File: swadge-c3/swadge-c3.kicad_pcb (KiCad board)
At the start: 2 copper layers, 62 parts, among them J1 USB_B_Micro, SW1 SW_SPDT, SW2 4-1437565-2, SW3 4-1437565-2, SW4 4-1437565-2, SW5 4-1437565-2, SW6 4-1437565-2, SW7 4-1437565-2, SW8 4-1437565-2, SW9 4-1437565-2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

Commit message: Updated schematic
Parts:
- added C21: 2.2u, Swadge_Parts:C_0603_1608Metric, F.Cu at (169.8, 122.4)
- added D7: WS2812B, Swadge_Parts:LED_WS2812B_PLCC4_5.0x5.0mm_P3.2mm, F.Cu at (171.8, 117.9)
- added D8: WS2812B, Swadge_Parts:LED_WS2812B_PLCC4_5.0x5.0mm_P3.2mm, F.Cu at (179.8, 117.9)
- C10: value 0.1uF -> 10uF
- C11: value 1uF -> 0.1uF
- C12: value 1u -> 1uF
- C16: value 2.2u -> 1u
- C17: value 10u -> 2.2u
- C18: value 0.01u -> 10u
- C19: value 0.1u -> 0.01u
- C20: value 2.2u -> 0.1u
- C9: value 10uF -> 1u
- R12: value 10K -> 390k
- R9: value 390k -> 10K
- SW1: value SW_SPDT -> 4-1437565-2; footprint Swadge_Parts:SW_SPDT_PCM12 -> Swadge_Parts:SW_4-1437565-2
- SW9: value 4-1437565-2 -> SW_SPDT; footprint Swadge_Parts:SW_4-1437565-2 -> Swadge_Parts:SW_SPDT_PCM12
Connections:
- C11 pad 1: EN -> +3V3
- C12 pad 1: Net-(C12-Pad1) -> EN
- C12 pad 2: Net-(C12-Pad2) -> GND
- C14 pad 1: GND -> Net-(C14-Pad1)
- C14 pad 2: +3V3 -> Net-(C14-Pad2)
- C16 pad 2: Net-(C16-Pad2) -> +3V3
- C20 pad 2: Net-(C19-Pad2) -> Net-(C20-Pad2)
- C8 pad 1: GND -> +3V3
- C8 pad 2: +5V -> GND
- C9 pad 1: +3V3 -> GND
- C9 pad 2: GND -> +5V
- D6 pad 2: LED_OUT -> Net-(D6-Pad2)
- R10 pad 2: IO8_SCL -> IO9_SDA
- R11 pad 1: +3V3 -> GND
- R11 pad 2: IO9_SDA -> IO10_RES
- R12 pad 2: (no net) -> Net-(R12-Pad2)
- R9 pad 1: GND -> +3V3
- R9 pad 2: Net-(R9-Pad2) -> IO8_SCL
- SW1 pad 1: Net-(BT2-Pad1) -> IO3_SW1
- SW1 pad 2: +3V3 -> IO3_SW1
- SW1 pad 3: Net-(SW1-Pad3) -> GND
- SW2 pad 1: IO3_SW1 -> IO0_SW2
- SW2 pad 2: IO3_SW1 -> IO0_SW2
- SW3 pad 1: IO5_SW5 -> IO1_SW3
- SW3 pad 2: IO5_SW5 -> IO1_SW3
- SW4 pad 1: IO1_SW2 -> IO4_SW4
- SW4 pad 2: IO1_SW2 -> IO4_SW4
- SW5 pad 1: IO7_SW6 -> IO5_SW5
- SW5 pad 2: IO7_SW6 -> IO5_SW5
- SW6 pad 1: IO10_SW3 -> IO7_SW6
- SW6 pad 2: IO10_SW3 -> IO7_SW6
- SW8 pad 1: IO4_SW4 -> IO19_SW8
- SW8 pad 2: IO4_SW4 -> IO19_SW8
- SW9 pad 1: IO19_SW8 -> Net-(BT2-Pad1)
- SW9 pad 2: IO19_SW8 -> +3V3
- SW9 pad 3: GND -> Net-(SW9-Pad3)
- U2 pad 2: Net-(SW1-Pad3) -> Net-(SW9-Pad3)
- U3 pad 12: IO10_RES -> IO0_SW2
- U3 pad 13: IO1_SW2 -> IO1_SW3
- U3 pad 16: IO10_SW3 -> IO10_RES
- U4 pad A10: IO18_SW7 -> IO5_SW5
- U4 pad A12: IO2_MIC -> IO6_BZR
- U4 pad A13: IO6_BZR -> IO7_SW6
- U4 pad A14: IO4_SW4 -> IO18_SW7
- U4 pad A17: IO5_SW5 -> IO19_SW8
- U4 pad A5: IO3_SW1 -> IO2_MIC
- U4 pad A6: IO1_SW2 -> IO3_SW1
- U4 pad A7: IO10_SW3 -> IO0_SW2
- U4 pad A9: IO7_SW6 -> IO1_SW3
- U4 pad B10: IO19_SW8 -> IO5_SW5
- U4 pad B12: IO2_MIC -> IO6_BZR
- U4 pad B13: IO6_BZR -> IO7_SW6
- U4 pad B14: IO4_SW4 -> IO18_SW7
- U4 pad B17: IO5_SW5 -> IO19_SW8
- U4 pad B5: IO3_SW1 -> IO2_MIC
- U4 pad B6: IO1_SW2 -> IO3_SW1
- U4 pad B7: IO10_SW3 -> IO0_SW2
- U4 pad B9: IO7_SW6 -> IO4_SW4
- U5 pad 2: Net-(C12-Pad1) -> Net-(C13-Pad1)
- U5 pad 26: Net-(R9-Pad2) -> Net-(R12-Pad2)
- U5 pad 27: Net-(C16-Pad2) -> Net-(C17-Pad2)
- U5 pad 28: Net-(C17-Pad2) -> Net-(C18-Pad2)
- U5 pad 3: Net-(C12-Pad2) -> Net-(C13-Pad2)
- U5 pad 4: Net-(C13-Pad1) -> Net-(C14-Pad1)
- U5 pad 5: Net-(C13-Pad2) -> Net-(C14-Pad2)
- U7 pad 3: Net-(C18-Pad2) -> Net-(C19-Pad2)
- U7 pad 7: Net-(C19-Pad2) -> Net-(C20-Pad2)

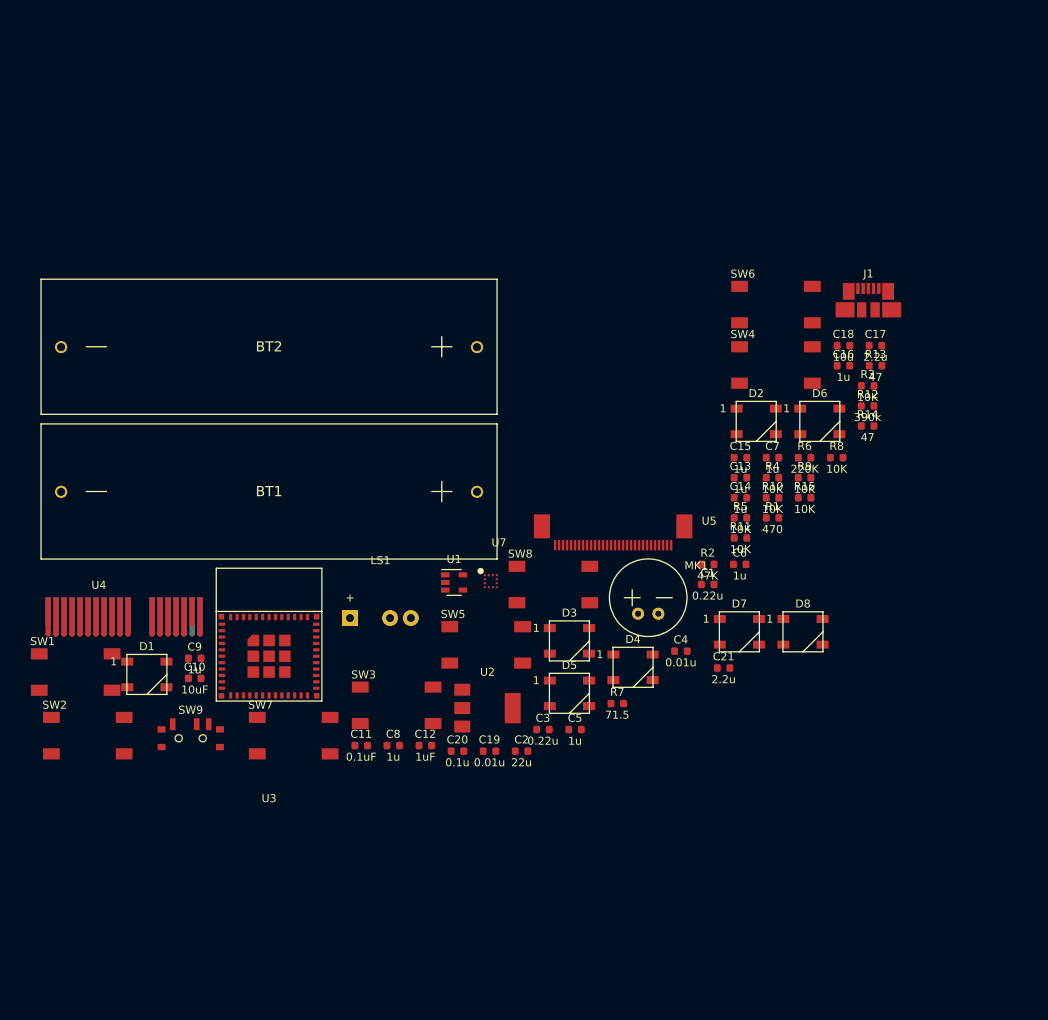
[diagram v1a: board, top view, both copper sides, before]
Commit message: Edited schematic, started layout
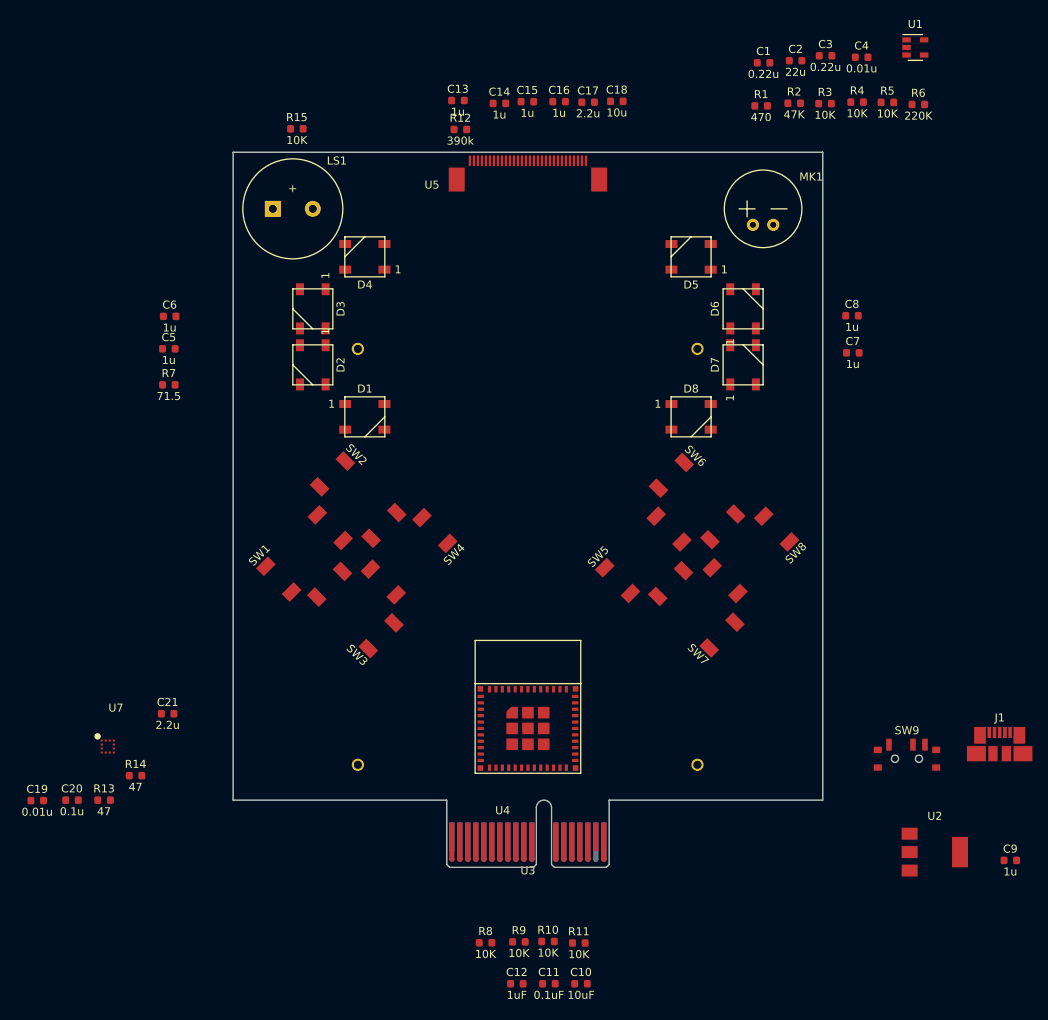
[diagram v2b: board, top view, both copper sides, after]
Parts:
- BT1, BT2: moved to B.Cu
- LS1: footprint Swadge_Parts:Buzzer_12x9.5RM7.6 -> Swadge_Parts:Buzzer_12.5x7.5
- moved R13 110.7 mm to (92.4, 138.9)
- moved C9 105.0 mm to (205.7, 146.4)
- moved R14 101.4 mm to (96.3, 135.8)
- moved U6 99.2 mm to (200.3, 109.2)
- moved C2 92.9 mm to (178.8, 46.5)
- moved C3 91.3 mm to (182.6, 45.9)
- moved SW9 89.6 mm to (192.8, 133.4)
- moved U1 88.3 mm to (193.8, 44.8)
- moved C8 78.6 mm to (185.9, 78.4)
- moved R15 78.5 mm to (116.5, 55.0)
- moved C6 77.7 mm to (100.6, 78.4)
- moved C4 77.6 mm to (187.1, 46.0)
- moved R8 74.9 mm to (140.1, 156.7)
- moved C21 69.7 mm to (100.4, 128.1)
- moved C5 69.6 mm to (100.5, 82.5)
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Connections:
- R10 pad 2: IO9_SDA -> IO9_SW6
- R11 pad 2: IO10_RES -> IO10_SW1
- R13 pad 2: IO8_SCL -> IO0_SCL
- R14 pad 2: IO9_SDA -> IO3_SDA
- R9 pad 2: IO8_SCL -> IO8_SW5
- SW1 pad 1: IO3_SW1 -> IO10_SW1
- SW1 pad 2: IO3_SW1 -> IO10_SW1
- SW1 pad 3: GND -> +3V3
- SW1 pad 4: GND -> +3V3
- SW2 pad 1: IO0_SW2 -> IO4_SW2
- SW2 pad 2: IO0_SW2 -> IO4_SW2
- SW3 pad 1: IO1_SW3 -> IO5_SW3
- SW3 pad 2: IO1_SW3 -> IO5_SW3
- SW4 pad 1: IO4_SW4 -> IO7_SW4
- SW4 pad 2: IO4_SW4 -> IO7_SW4
- SW5 pad 1: IO5_SW5 -> IO8_SW5
- SW5 pad 2: IO5_SW5 -> IO8_SW5
- SW6 pad 1: IO7_SW6 -> IO9_SW6
- SW6 pad 2: IO7_SW6 -> IO9_SW6
- U3 pad 12: IO0_SW2 -> IO0_SCL
- U3 pad 13: IO1_SW3 -> IO1_RES
- U3 pad 16: IO10_RES -> IO10_SW1
- U3 pad 18: IO4_SW4 -> IO4_SW2
- U3 pad 19: IO5_SW5 -> IO5_SW3
- U3 pad 21: IO7_SW6 -> IO7_SW4
- U3 pad 22: IO8_SCL -> IO8_SW5
- U3 pad 23: IO9_SDA -> IO9_SW6
- U3 pad 6: IO3_SW1 -> IO3_SDA
- U4 pad A10: IO5_SW5 -> IO5_SW3
- U4 pad A13: IO7_SW6 -> IO7_SW4
- U4 pad A2: IO8_SCL -> IO8_SW5
- U4 pad A3: IO9_SDA -> IO9_SW6
- U4 pad A4: IO10_RES -> IO10_SW1
- U4 pad A6: IO3_SW1 -> IO3_SDA
- U4 pad A7: IO0_SW2 -> IO0_SCL
- U4 pad A9: IO1_SW3 -> IO1_RES
- U4 pad B10: IO5_SW5 -> IO5_SW3
- U4 pad B13: IO7_SW6 -> IO7_SW4
- U4 pad B2: IO8_SCL -> IO8_SW5
- U4 pad B3: IO9_SDA -> IO9_SW6
- U4 pad B4: IO10_RES -> IO10_SW1
- U4 pad B6: IO3_SW1 -> IO3_SDA
- U4 pad B7: IO0_SW2 -> IO0_SCL
- U4 pad B9: IO4_SW4 -> IO4_SW2
- U5 pad 14: IO10_RES -> IO1_RES
- U5 pad 18: IO8_SCL -> IO0_SCL
- U5 pad 19: IO9_SDA -> IO3_SDA
- U5 pad 20: IO9_SDA -> IO3_SDA
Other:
- board outline added: 73.7 x 89.4 mm

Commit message: layout updates
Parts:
- moved C19 45.0 mm to (127.2, 126.2)
- moved R13 40.5 mm to (131.5, 128.2)
- moved C20 38.9 mm to (126.0, 129.0)
- moved U7 36.1 mm to (128.8, 128.6), turned to 270 degrees
- moved C9 35.7 mm to (171.4, 136.7)
- moved R14 35.5 mm to (130.5, 126.2)
- moved R7 31.3 mm to (130.0, 97.5), turned to 270 degrees
- moved U2 29.3 mm to (171.4, 129.8), turned to 90 degrees
- moved C21 26.8 mm to (127.0, 130.8)
- moved J1 24.9 mm to (179.6, 134.2), turned to 90 degrees
- moved R15 17.9 mm to (111.0, 72.0), turned to 270 degrees
- moved SW9 16.9 mm to (179.9, 122.5), turned to 90 degrees
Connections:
- C19 pad 2: Net-(C19-Pad2) -> +3V3
- C20 pad 2: Net-(C20-Pad2) -> +3V3
- C21 pad 2: Net-(C20-Pad2) -> +3V3
- J1 pad 2: (no net) -> Net-(J1-Pad2)
- J1 pad 3: (no net) -> Net-(J1-Pad3)
- J1 pad 4: (no net) -> Net-(J1-Pad4)
- U3 pad 10: (no net) -> Net-(U3-Pad10)
- U3 pad 15: (no net) -> Net-(U3-Pad15)
- U3 pad 17: (no net) -> Net-(U3-Pad17)
- U3 pad 24: (no net) -> Net-(U3-Pad24)
- U3 pad 25: (no net) -> Net-(U3-Pad25)
- U3 pad 28: (no net) -> Net-(U3-Pad28)
- U3 pad 29: (no net) -> Net-(U3-Pad29)
- U3 pad 32: (no net) -> Net-(U3-Pad32)
- U3 pad 33: (no net) -> Net-(U3-Pad33)
- U3 pad 34: (no net) -> Net-(U3-Pad34)
- U3 pad 35: (no net) -> Net-(U3-Pad35)
- U3 pad 4: (no net) -> Net-(U3-Pad4)
- U3 pad 7: (no net) -> Net-(U3-Pad7)
- U3 pad 9: (no net) -> Net-(U3-Pad9)
- U5 pad 7: (no net) -> Net-(U5-Pad7)
- U7 pad 10: (no net) -> Net-(U7-Pad10)
- U7 pad 11: (no net) -> Net-(U7-Pad11)
- U7 pad 3: Net-(C19-Pad2) -> +3V3
- U7 pad 5: (no net) -> Net-(U7-Pad5)
- U7 pad 6: (no net) -> Net-(U7-Pad6)
- U7 pad 7: Net-(C20-Pad2) -> +3V3
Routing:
- net +3V3: track 0.00 -> 203.9 mm, vias 0 -> 1
- net IO6_BZR: track 0.00 -> 110.2 mm, vias 0 -> 3
- net IO9_SW6: track 0.00 -> 83.0 mm, vias 0 -> 4
- net IO10_SW1: track 0.00 -> 76.2 mm, vias 0 -> 3
- net RX: track 0.00 -> 75.2 mm, vias 0 -> 5
- net IO4_SW2: track 0.00 -> 63.5 mm, vias 0 -> 2
- net IO8_SW5: track 0.00 -> 62.8 mm, vias 0 -> 4
- net IO5_SW3: track 0.00 -> 59.7 mm, vias 0 -> 3
- net IO7_SW4: track 0.00 -> 57.5 mm, vias 0 -> 3
- net IO19_SW8: track 0.00 -> 57.0 mm, vias 0 -> 3
- net IO18_SW7: track 0.00 -> 52.5 mm, vias 0 -> 3
- net Net-(BT1-Pad1): track 0.00 -> 42.4 mm
- net Net-(D4-Pad2): track 0.00 -> 37.2 mm
- net +5V: track 0.00 -> 37.1 mm, vias 0 -> 1
- net IO3_SDA: track 0.00 -> 28.8 mm, vias 0 -> 3
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- added copper zone on B.Cu, net GND
- added copper zone on F.Cu, net GND
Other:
- net class PWR added: clearance 0.2, trace_width 0.4, via_dia 0.8, via_drill 0.4

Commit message: Update layout
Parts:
- moved C10 39.5 mm to (134.5, 126.5), turned to 180 degrees
- moved C11 39.3 mm to (134.5, 125.0), turned to 180 degrees
- moved R10 36.7 mm to (154.5, 120.5), turned to 180 degrees
- moved C12 35.2 mm to (134.5, 128.0), turned to 180 degrees
- moved R9 33.7 mm to (156.0, 125.0), turned to 180 degrees
- moved C18 28.2 mm to (132.0, 65.5)
- moved R11 28.0 mm to (133.0, 136.0), turned to 270 degrees
- moved R8 27.8 mm to (134.5, 129.5), turned to 180 degrees
- moved C5 27.0 mm to (127.0, 87.5)
- moved C13 26.0 mm to (158.5, 65.5), turned to 180 degrees
- moved C15 22.6 mm to (158.5, 70.0), turned to 180 degrees
- moved C8 22.2 mm to (164.0, 74.5), turned to 180 degrees
- moved C17 22.2 mm to (135.5, 65.5)
- moved C6 21.4 mm to (122.0, 79.5), turned to 270 degrees
- moved C16 19.3 mm to (155.0, 70.0), turned to 180 degrees
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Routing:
- net +3V3: track 203.9 -> 319.2 mm, vias 1 -> 9
- net LED_OUT: track 9.40 -> 68.8 mm, vias 1 -> 4
- net GND: track 8.19 -> 53.2 mm, vias 8 -> 16
- net IO3_SDA: track 28.8 -> 43.0 mm, vias 3 -> 4
- net IO0_SCL: track 26.8 -> 40.0 mm
- net Net-(R12-Pad2): track 0.00 -> 12.6 mm
- net Net-(C13-Pad1): track 0.00 -> 11.8 mm
- net Net-(C13-Pad2): track 0.00 -> 11.1 mm
- net Net-(C18-Pad2): track 0.00 -> 10.7 mm
- net Net-(C14-Pad1): track 0.00 -> 9.71 mm
- net EN: track 0.00 -> 9.44 mm, vias 0 -> 2
- net Net-(C14-Pad2): track 0.00 -> 8.71 mm
- net Net-(C17-Pad2): track 0.00 -> 7.91 mm
- net Net-(D1-Pad4): track 8.37 -> 4.83 mm
- net RX: track 75.2 -> 77.4 mm
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
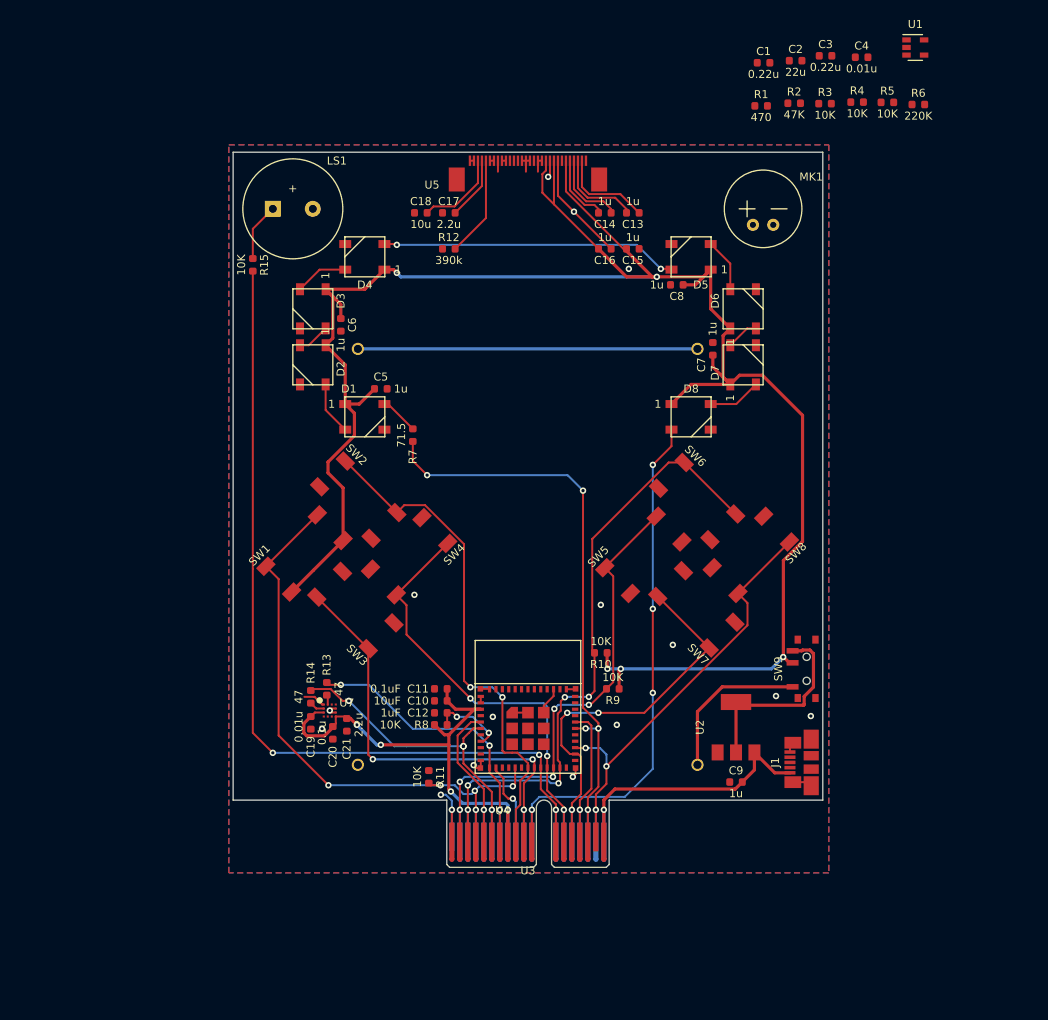
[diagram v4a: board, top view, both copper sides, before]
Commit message: Complete PCB routing
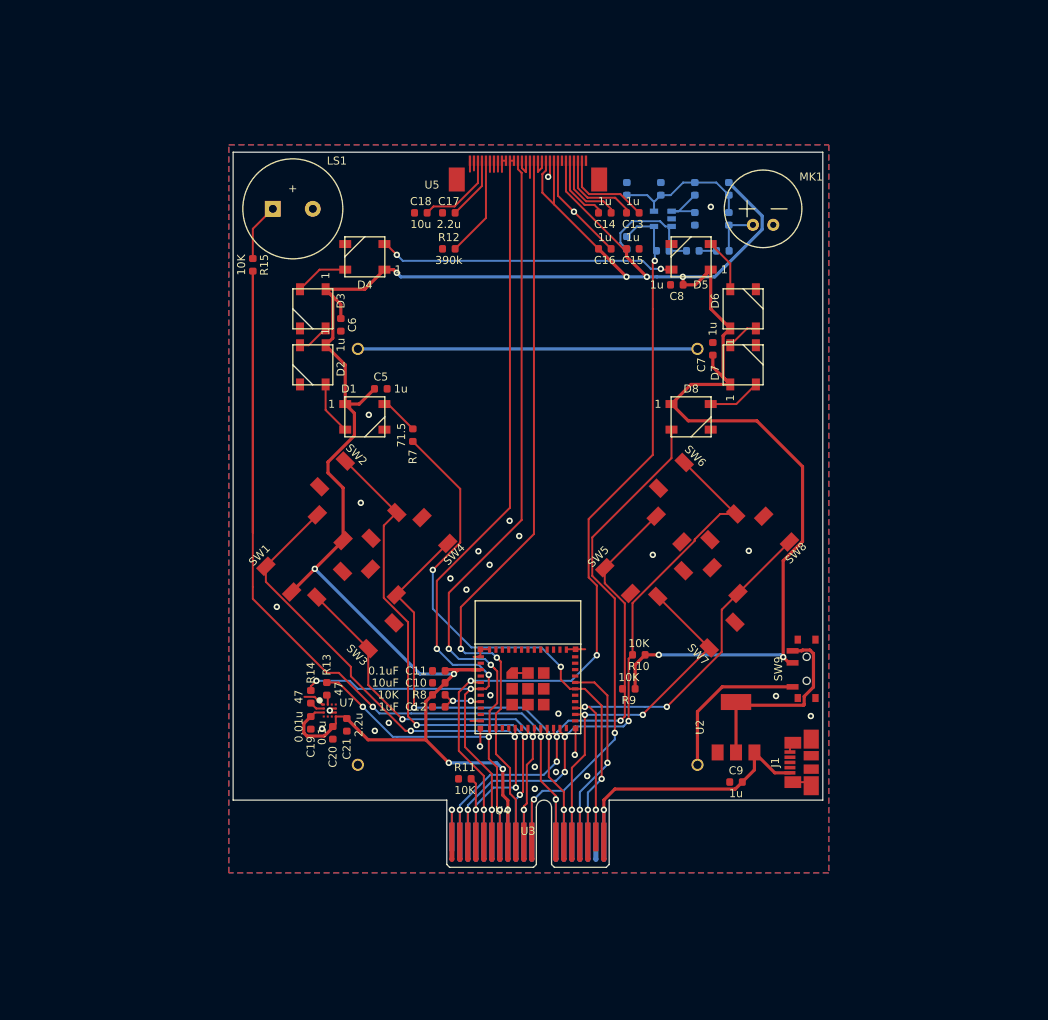
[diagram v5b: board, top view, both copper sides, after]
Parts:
- C1, C2, C3, C4, R1, R2, R3, R4, R5, R6, U1: moved to B.Cu
- moved U1 38.1 mm to (162.2, 66.2), turned to 180 degrees
- moved C4 37.4 mm to (157.8, 69.2), turned to 270 degrees
- moved R6 36.8 mm to (162.2, 70.2)
- moved R4 27.7 mm to (166.0, 70.2)
- moved C3 27.6 mm to (169.8, 70.2)
- moved C2 26.5 mm to (157.8, 62.5), turned to 270 degrees
- moved R5 24.6 mm to (170.5, 66.2), turned to 270 degrees
- moved R3 21.7 mm to (166.2, 66.2), turned to 90 degrees
- moved C1 20.3 mm to (162.0, 62.5), turned to 270 degrees
- moved R2 16.4 mm to (166.2, 62.5), turned to 90 degrees
- moved R1 11.1 mm to (170.5, 62.5), turned to 270 degrees
- moved U3 4.95 mm to (145.4, 125.0)
- moved R10 4.76 mm to (159.2, 120.8)
- moved R11 4.51 mm to (137.5, 136.2), turned to 0 degrees
- moved R8 3.76 mm to (134.2, 125.8)
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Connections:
- U4 pad A9: IO1_RES -> IO4_SW2
- U4 pad B9: IO4_SW2 -> IO1_RES
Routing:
- net IO2_MIC: track 22.0 -> 105.9 mm, vias 1 -> 4
- net IO1_RES: track 10.5 -> 94.2 mm, vias 1 -> 2
- net IO0_SCL: track 40.0 -> 121.4 mm, vias 3 -> 5
- net IO3_SDA: track 43.0 -> 122.8 mm, vias 4 -> 5
- net +3V3: track 319.2 -> 356.1 mm, vias 9 -> 11
- net IO6_BZR: track 110.2 -> 137.3 mm
- net Net-(C1-Pad2): track 0.00 -> 18.1 mm
- net Net-(C4-Pad2): track 0.00 -> 15.0 mm
- net GND: track 53.2 -> 62.7 mm, vias 16 -> 29
- net Net-(R2-Pad1): track 0.00 -> 6.70 mm
- net TX: track 21.5 -> 28.2 mm, vias 1 -> 2
- net Net-(C3-Pad2): track 0.00 -> 6.26 mm
- net IO9_SW6: track 84.2 -> 78.4 mm, vias 5 -> 4
- net IO7_SW4: track 57.5 -> 61.7 mm
- net RX: track 77.4 -> 73.5 mm, vias 5 -> 4
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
